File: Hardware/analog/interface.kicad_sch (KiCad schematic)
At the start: 28 parts

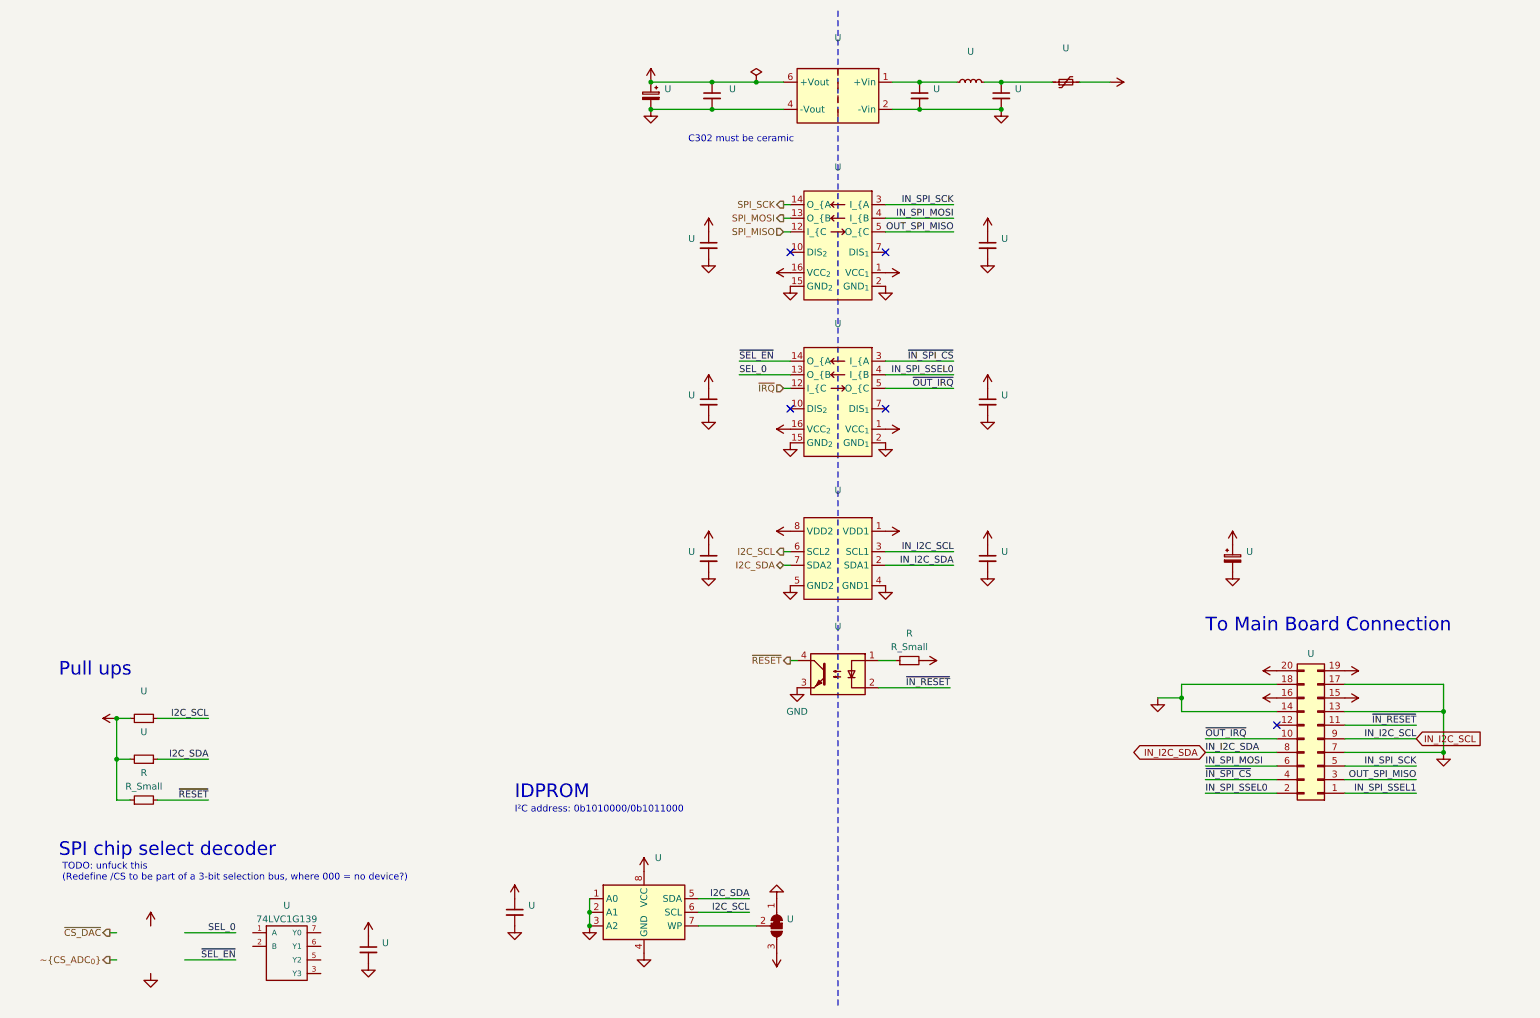
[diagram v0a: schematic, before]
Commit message: Mostly finished up analog load board
- Finished routing most signals

- Connected relay drive to bonus I2C GPIO controller, and routed the
  rest of the voltage sense stuff

- Routed the reset signal to the DAC, so that when the board is reset,
  the current output will be reset to zero as well without processor
  intervention

- Replaced most passives with 0603/1608 size
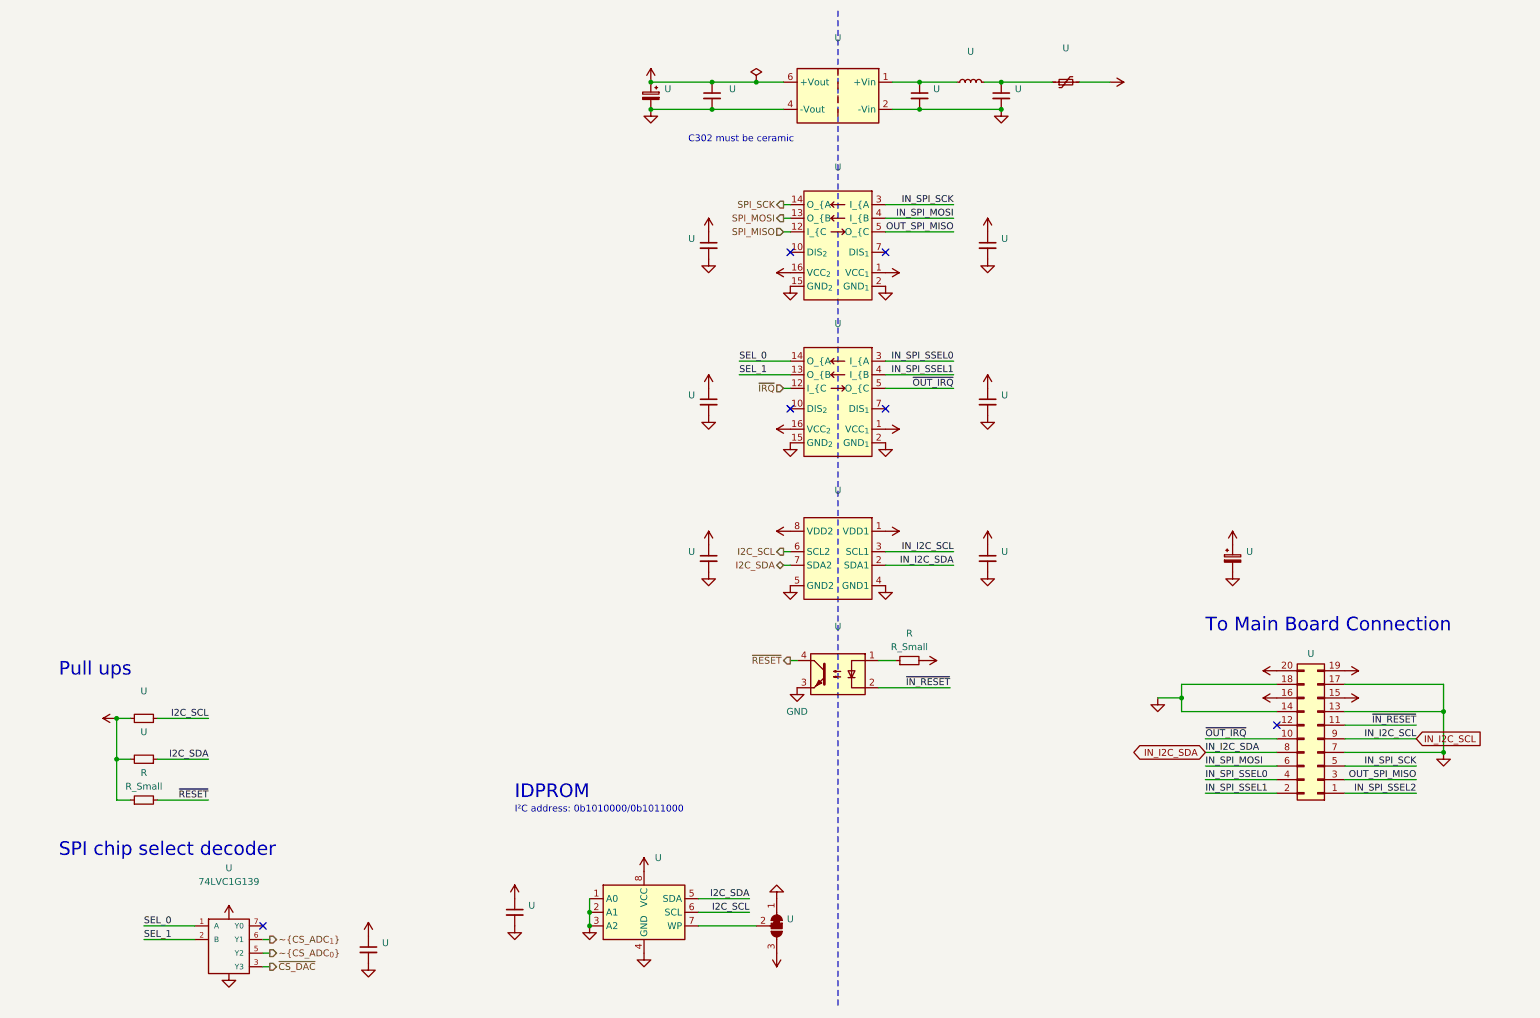
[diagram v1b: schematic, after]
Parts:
- U: MPN RMC1/10-222JTP -> (none)
- U: MPN A750EK476M1EAAE040 -> A768EB336M1GLAE045
- U: MPN CL21A475KAQNNNF -> (none)
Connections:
- net VCC is gone; now on net +3V3: U.8 (VCC)
- net ~{IN_SPI_CS} is gone; now on net IN_SPI_SSEL0: U.3 (I_{A), U.4 (Pin_4)
- net ~{SEL_EN} is gone; now on net SEL_0: U.14 (O_{A)
- net IN_SPI_SSEL0: no longer U.2 (Pin_2), U.4 (I_{B)
- net IN_SPI_SSEL1: now also U.2 (Pin_2), U.4 (I_{B); no longer U.1 (Pin_1)
- net SEL_0: now also U.1 (A); no longer U.13 (O_{B)
- net ~{CS_ADC_{0}}: now also U.5 (Y2)
- net ~{CS_DAC}: now also U.3 (Y3)
- net SEL_1: now reaches U.2 (B)
- net SEL_1: now also U.13 (O_{B)
- net ~{CS_ADC_{1}}: now reaches U.6 (Y1)
- new net IN_SPI_SSEL2: U.1 (Pin_1)
- no-connect marks 5 -> 6
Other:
- note removed: "TODO: unfuck this (Redefine /CS to be part of a 3-bit selection bus, where 000 = no device?)"
- moved on the sheet: U

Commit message: Analog board changes
- Switched IDPROM for a TSSOP-8 package, rather than the SOIC-8 which is
  basically unobtanium

- Minor layout unrelated tweaks
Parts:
- U: symbol Memory_EEPROM:AT24CS32-SSHM -> Memory_EEPROM:AT24CS32-XHM
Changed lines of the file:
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@@
     (pin "1")
   )
-  (symbol (lib_id "Memory_EEPROM:AT24CS32-SSHM") (at 123.825 180.34 0) (unit 1)
+  (symbol (lib_id "Memory_EEPROM:AT24CS32-XHM") (at 123.825 180.34 0) (unit 1)
     (in_bom yes) (on_board yes) (fields_autoplaced)
     (default_instance (reference "U") (unit 1) (value "") (footprint ""))

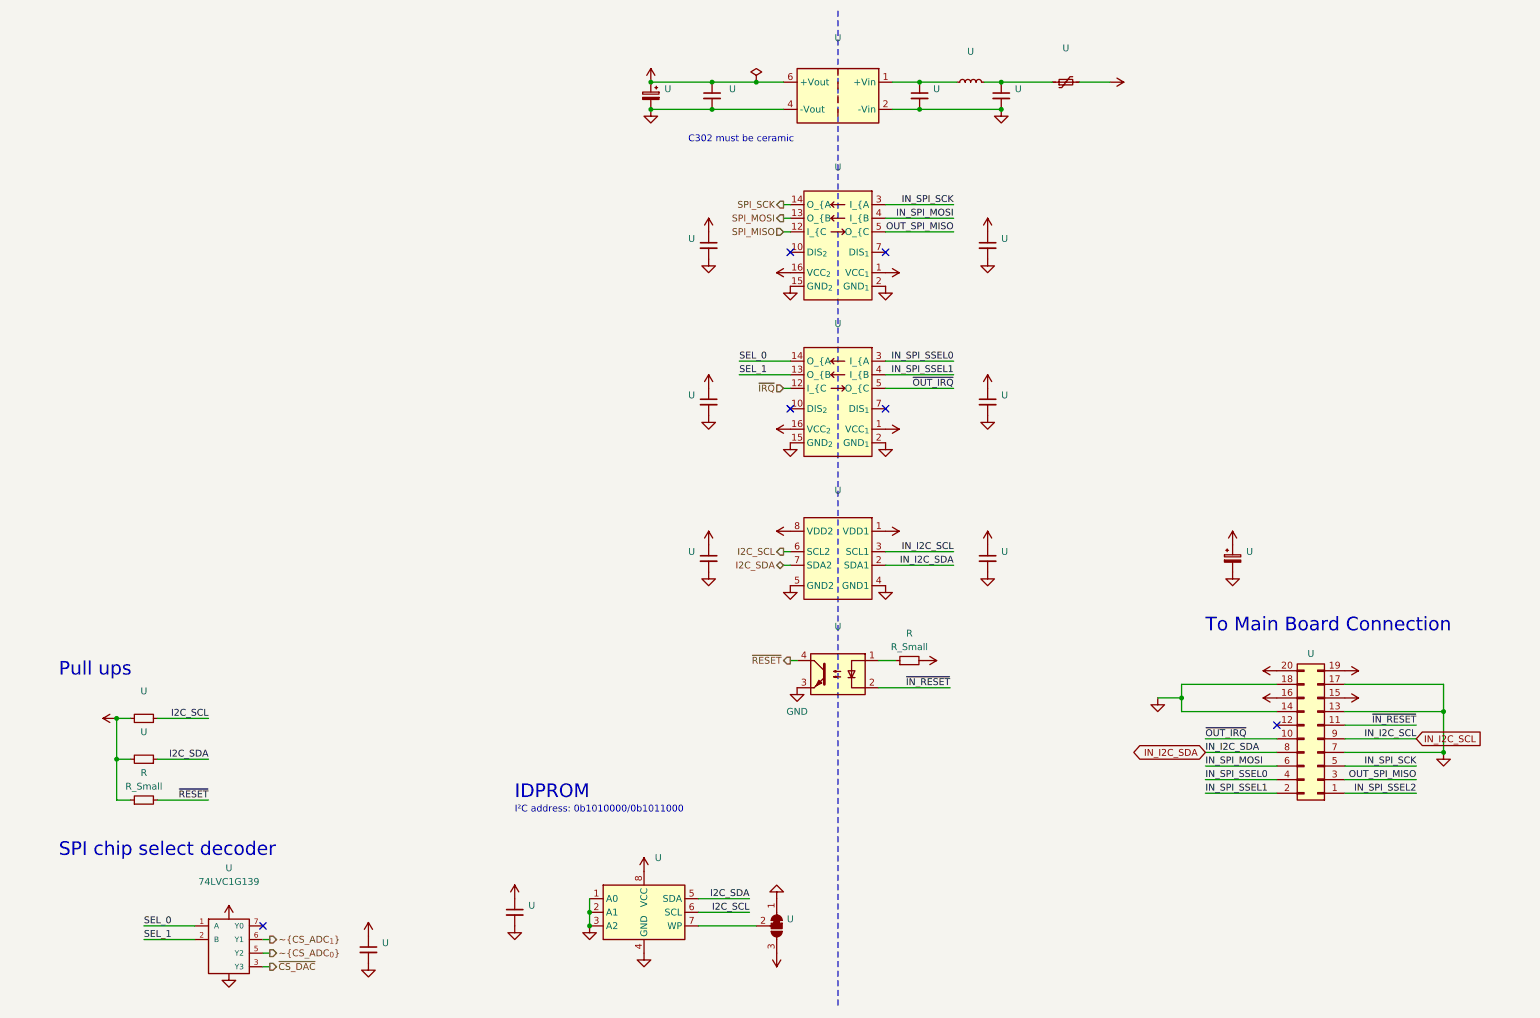
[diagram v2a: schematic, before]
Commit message: Temperature sensing & cleanup for analog board
- Added the auxiliary temperature sensing ADC, and routed it to the
  analog temperature sensors on the front and rear of the MOSFET
  heatsink

- Added an LM75 sensor to measure the analog board ambient temperature
  (for better temperature control/fan control)

  This may end up being a DNP item if it's not really useful or
  otherwise necessary.

- Fixes to a few symbols (namely pin directions) to pass ERC
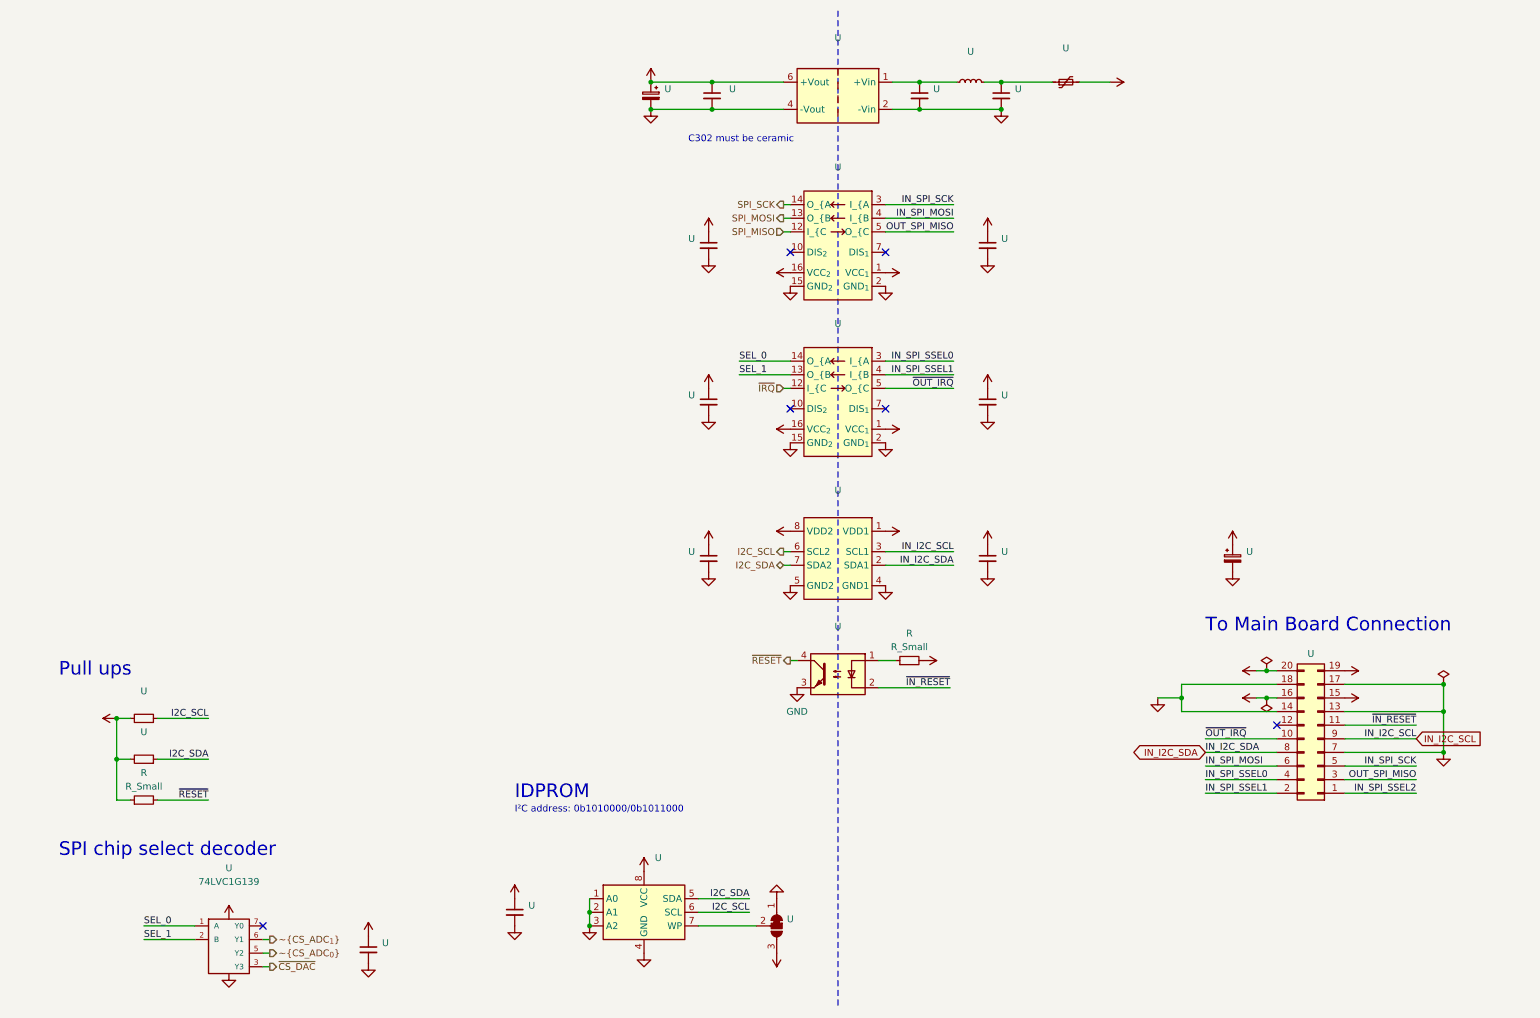
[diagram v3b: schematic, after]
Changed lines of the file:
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@@
   (junction (at 175.26 25.4) (diameter 0) (color 0 0 0 0)
   )
-  (junction (at 144.78 25.4) (diameter 0) (color 0 0 0 0)
-  )
   (junction (at 125.095 30.48) (diameter 0) (color 0 0 0 0)
   )
@@
   (junction (at 136.525 30.48) (diameter 0) (color 0 0 0 0)
   )
+  (junction (at 240.03 140.335) (diameter 0) (color 0 0 0 0)
+  )
   (junction (at 273.05 150.495) (diameter 0) (color 0 0 0 0)
+  )
+  (junction (at 273.05 137.795) (diameter 0) (color 0 0 0 0)
+  )
+  (junction (at 240.03 135.255) (diameter 0) (color 0 0 0 0)
   )
   (no_connect (at 151.13 57.15))
@@
     (stroke (width 0) (type default))
   )
-  (wire (pts (xy 144.78 25.4) (xy 149.86 25.4))
-    (stroke (width 0) (type default))
-  )
   (wire (pts (xy 175.26 25.4) (xy 182.245 25.4))
     (stroke (width 0) (type default))
@@
     (stroke (width 0) (type default))
   )
+  (wire (pts (xy 238.125 135.255) (xy 240.03 135.255))
+    (stroke (width 0) (type default))
+  )
   (wire (pts (xy 25.4 151.765) (xy 25.4 159.385))
     (stroke (width 0) (type default))
@@
     (stroke (width 0) (type default))
   )
-  (wire (pts (xy 136.525 25.4) (xy 144.78 25.4))
+  (wire (pts (xy 136.525 25.4) (xy 149.86 25.4))
     (stroke (width 0) (type default))
   )
@@
     (stroke (width 0) (type default))
   )
+  (wire (pts (xy 240.03 135.255) (xy 241.935 135.255))
+    (stroke (width 0) (type default))
+  )
   (wire (pts (xy 25.4 151.765) (xy 27.94 151.765))
     (stroke (width 0) (type default))
@@
     (stroke (width 0) (type default))
   )
+  (wire (pts (xy 240.03 140.335) (xy 241.935 140.335))
+    (stroke (width 0) (type default))
+  )
   (wire (pts (xy 53.975 190.5) (xy 52.705 190.5))
+    (stroke (width 0) (type default))
+  )
+  (wire (pts (xy 238.125 140.335) (xy 240.03 140.335))
     (stroke (width 0) (type default))
   )
@@
     (pin "1")
   )
+  (symbol (lib_id "power:PWR_FLAG") (at 240.03 135.255 0) (unit 1)
+    (in_bom yes) (on_board yes) (fields_autoplaced)
+    (default_instance (reference "#FLG") (unit 1) (value "PWR_FLAG") (footprint ""))
+    (property "Reference" "#FLG" (id 0) (at 240.03 133.35 0)
+      (effects (font (size 1.27 1.27)) hide)
+    )
+    (property "Value" "PWR_FLAG" (id 1) (at 240.03 132.08 0)
+      (effects (font (size 1.27 1.27)) hide)
+    )
+    (property "Footprint" "" (id 2) (at 240.03 135.255 0)
+      (effects (font (size 1.27 1.27)) hide)
+    )
+    (property "Datasheet" "~" (id 3) (at 240.03 135.255 0)
+      (effects (font (size 1.27 1.27)) hide)
+    )
+    (pin "1")
+  )
   (symbol (lib_id "Memory_EEPROM:AT24CS32-XHM") (at 123.825 180.34 0) (unit 1)
     (in_bom yes) (on_board yes) (fields_autoplaced)
@@
     (pin "1")
   )
+  (symbol (lib_id "power:PWR_FLAG") (at 240.03 140.335 180) (unit 1)
+    (in_bom yes) (on_board yes) (fields_autoplaced)
+    (default_instance (reference "#FLG") (unit 1) (value "PWR_FLAG") (footprint ""))
+    (property "Reference" "#FLG" (id 0) (at 240.03 142.24 0)
+      (effects (font (size 1.27 1.27)) hide)
+    )
+    (property "Value" "PWR_FLAG" (id 1) (at 240.03 144.78 0)
+      (effects (font (size 1.27 1.27)) hide)
+    )
+    (property "Footprint" "" (id 2) (at 240.03 140.335 0)
+      (effects (font (size 1.27 1.27)) hide)
+    )
+    (property "Datasheet" "~" (id 3) (at 240.03 140.335 0)
+      (effects (font (size 1.27 1.27)) hide)
+    )
+    (pin "1")
+  )
   (symbol (lib_id "power:GND") (at 125.095 30.48 0) (unit 1)
     (in_bom yes) (on_board yes) (fields_autoplaced)
@@
     (pin "1")
   )
-  (symbol (lib_id "power:+3.3VP") (at 241.935 140.335 90) (unit 1)
-    (in_bom yes) (on_board yes)
-    (default_instance (reference "U") (unit 1) (value "") (footprint ""))
-    (property "Reference" "U" (id 0) (at 243.205 136.525 0)
-      (effects (font (size 1.27 1.27)) hide)
-    )
-    (property "Value" "" (id 1) (at 238.76 140.335 90)
-      (effects (font (size 1.27 1.27)) (justify left))
-    )
-    (property "Footprint" "" (id 2) (at 241.935 140.335 0)
-      (effects (font (size 1.27 1.27)) hide)
-    )
-    (property "Datasheet" "" (id 3) (at 241.935 140.335 0)
+  (symbol (lib_id "power:+3.3VP") (at 238.125 140.335 90) (unit 1)
+    (in_bom yes) (on_board yes)
+    (default_instance (reference "U") (unit 1) (value "") (footprint ""))
+    (property "Reference" "U" (id 0) (at 239.395 136.525 0)
+      (effects (font (size 1.27 1.27)) hide)
+    )
+    (property "Value" "" (id 1) (at 234.95 140.335 90)
+      (effects (font (size 1.27 1.27)) (justify left))
+    )
+    (property "Footprint" "" (id 2) (at 238.125 140.335 0)
+      (effects (font (size 1.27 1.27)) hide)
+    )
+    (property "Datasheet" "" (id 3) (at 238.125 140.335 0)
       (effects (font (size 1.27 1.27)) hide)
     )
@@
     (pin "1")
   )
+  (symbol (lib_id "power:PWR_FLAG") (at 273.05 137.795 0) (unit 1)
+    (in_bom yes) (on_board yes) (fields_autoplaced)
+    (default_instance (reference "#FLG") (unit 1) (value "PWR_FLAG") (footprint ""))
+    (property "Reference" "#FLG" (id 0) (at 273.05 135.89 0)
+      (effects (font (size 1.27 1.27)) hide)
+    )
+    (property "Value" "PWR_FLAG" (id 1) (at 273.05 134.62 0)
+      (effects (font (size 1.27 1.27)) hide)
+    )
+    (property "Footprint" "" (id 2) (at 273.05 137.795 0)
+      (effects (font (size 1.27 1.27)) hide)
+    )
+    (property "Datasheet" "~" (id 3) (at 273.05 137.795 0)
+      (effects (font (size 1.27 1.27)) hide)
+    )
+    (pin "1")
+  )
   (symbol (lib_id "power:GND2") (at 187.96 58.42 0) (unit 1)
     (in_bom yes) (on_board yes)
@@
     (pin "1")
   )
-  (symbol (lib_id "power:VBUS") (at 241.935 135.255 90) (unit 1)
-    (in_bom yes) (on_board yes)
-    (default_instance (reference "U") (unit 1) (value "") (footprint ""))
-    (property "Reference" "U" (id 0) (at 245.745 135.255 0)
-      (effects (font (size 1.27 1.27)) hide)
-    )
-    (property "Value" "" (id 1) (at 238.76 135.255 90)
-      (effects (font (size 1.27 1.27)) (justify left))
-    )
-    (property "Footprint" "" (id 2) (at 241.935 135.255 0)
-      (effects (font (size 1.27 1.27)) hide)
-    )
-    (property "Datasheet" "" (id 3) (at 241.935 135.255 0)
+  (symbol (lib_id "power:VBUS") (at 238.125 135.255 90) (unit 1)
+    (in_bom yes) (on_board yes)
+    (default_instance (reference "U") (unit 1) (value "") (footprint ""))
+    (property "Reference" "U" (id 0) (at 241.935 135.255 0)
+      (effects (font (size 1.27 1.27)) hide)
+    )
+    (property "Value" "" (id 1) (at 234.95 135.255 90)
+      (effects (font (size 1.27 1.27)) (justify left))
+    )
+    (property "Footprint" "" (id 2) (at 238.125 135.255 0)
+      (effects (font (size 1.27 1.27)) hide)
+    )
+    (property "Datasheet" "" (id 3) (at 238.125 135.255 0)
       (effects (font (size 1.27 1.27)) hide)
     )
@@
     (pin "2")
   )
-  (symbol (lib_id "power:PWR_FLAG") (at 144.78 25.4 0) (unit 1)
-    (in_bom yes) (on_board yes) (fields_autoplaced)
-    (default_instance (reference "U") (unit 1) (value "") (footprint ""))
-    (property "Reference" "U" (id 0) (at 144.78 23.495 0)
-      (effects (font (size 1.27 1.27)) hide)
-    )
-    (property "Value" "" (id 1) (at 144.78 19.685 0)
-      (effects (font (size 1.27 1.27)))
-    )
-    (property "Footprint" "" (id 2) (at 144.78 25.4 0)
-      (effects (font (size 1.27 1.27)) hide)
-    )
-    (property "Datasheet" "~" (id 3) (at 144.78 25.4 0)
-      (effects (font (size 1.27 1.27)) hide)
-    )
-    (pin "1")
-  )
   (symbol (lib_id "power:+3.3VP") (at 233.68 111.76 0) (unit 1)
